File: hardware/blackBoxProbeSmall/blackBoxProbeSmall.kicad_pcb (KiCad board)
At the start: 4 copper layers, 44 x 29 mm, 79 parts, among them J1 USB-ID, J2 JTAG_2X05, J3 JTAG_2X05, J4 DevBoardUartInput, Q1 Q_NMOS_DUAL, Q2 Q_PMOS_DUAL, U1 MCP1702-MB, U2 USBLC6-2, U3 STM32F103CBT, U4 74X2T45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

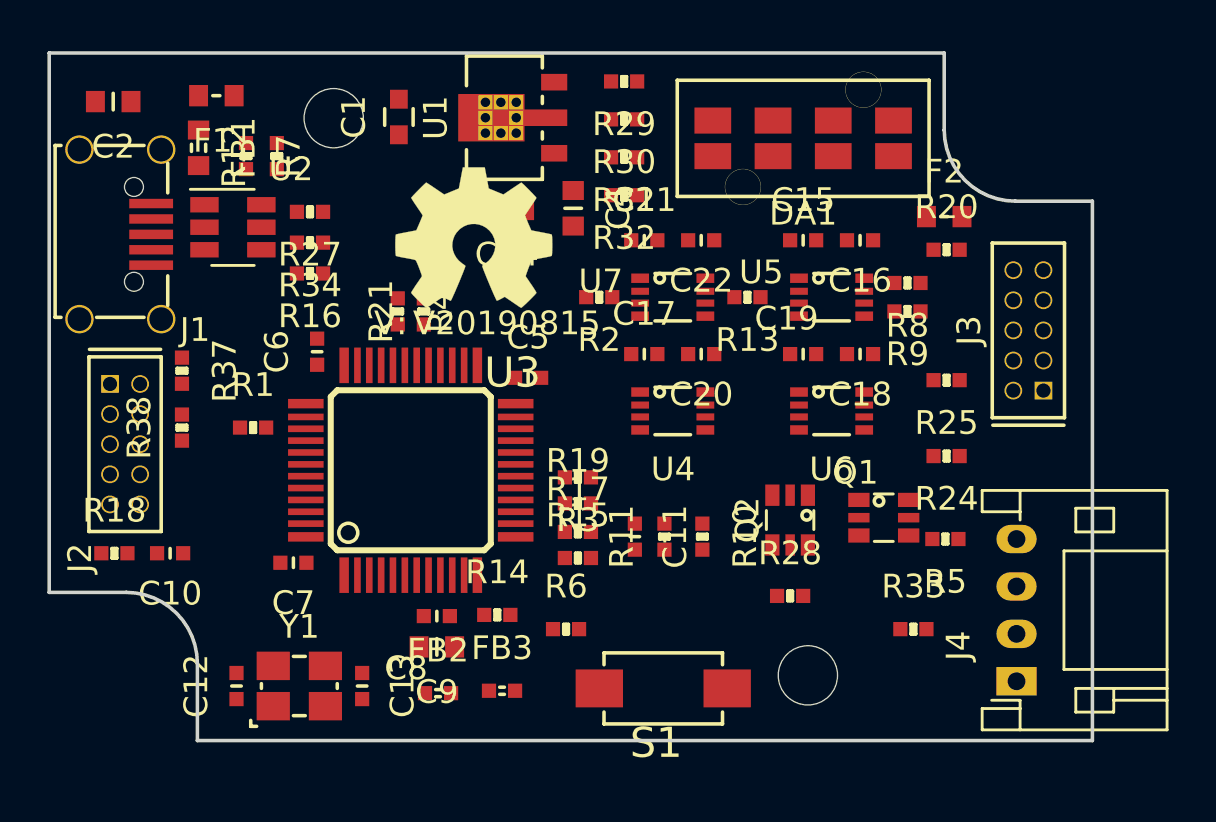
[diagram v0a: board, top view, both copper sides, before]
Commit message: initial component placement completed
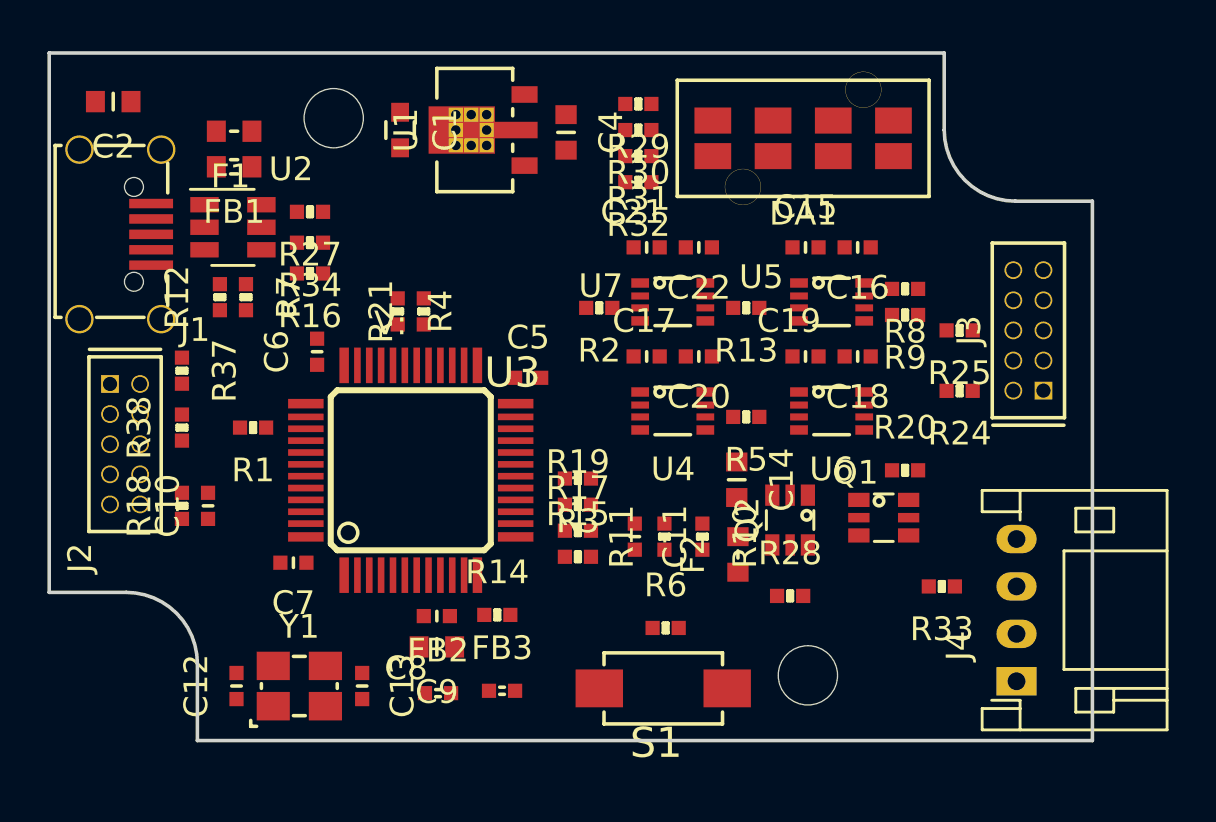
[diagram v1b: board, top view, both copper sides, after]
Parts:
- N1: moved to B.Cu
- moved F2 16.7 mm to (152.8, 106.0), turned to 90 degrees
- moved C14 15.0 mm to (152.7, 102.9), turned to 270 degrees
- moved R5 9.85 mm to (153.1, 100.2)
- moved R20 9.46 mm to (159.8, 102.5)
- moved R12 6.42 mm to (130.9, 95.2)
- moved R7 5.95 mm to (132.0, 95.2)
- moved R6 4.20 mm to (149.7, 109.2)
- moved R18 3.48 mm to (129.3, 104.0), turned to 90 degrees
- moved C4 3.21 mm to (145.5, 88.2)
- moved R24 2.80 mm to (162.1, 99.2)
- moved C10 2.56 mm to (130.4, 104.0), turned to 90 degrees
- moved R25 2.17 mm to (162.1, 96.6)
- moved R33 2.16 mm to (161.3, 107.4), turned to 180 degrees
- moved FB1 1.70 mm to (131.5, 89.7), turned to 180 degrees
- moved F1 1.68 mm to (131.5, 88.2)
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
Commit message: more layout
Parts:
- moved FB3 2.20 mm to (140.6, 111.8), turned to 270 degrees
- moved FB2 0.62 mm to (139.5, 111.8), turned to 270 degrees
- moved R16 0.30 mm to (134.7, 93.9)
- moved R27 0.11 mm to (134.7, 91.7)
- moved R34 0.11 mm to (134.7, 92.8)
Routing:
- net /VSS: track 0.00 -> 31.6 mm, vias 0 -> 10
- net /VUSB: track 0.00 -> 20.4 mm
- net Net-(C2-Pad2): track 0.00 -> 16.4 mm
- net /VDD: track 0.00 -> 8.06 mm, vias 0 -> 4
- net /VDDA: track 0.00 -> 4.61 mm
- net /VSSA: track 0.00 -> 4.52 mm
- net Net-(FB1-Pad2): track 0.00 -> 3.77 mm
- net Net-(R16-Pad2): track 0.00 -> 2.72 mm
- net /USB_D_C+: track 0.00 -> 2.52 mm
- net /USB_D_C-: track 0.00 -> 2.50 mm
- net Net-(F1-Pad2): track 0.00 -> 2.12 mm
- net Net-(R27-Pad2): track 0.00 -> 1.62 mm
- net /USB_V: track 0.00 -> 1.10 mm
- added copper zone on In2.Cu, net /VDD
- added copper zone on In1.Cu, net /VSS

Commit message: minor layout changes
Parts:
- moved R21 0.49 mm to (139.9, 95.6)
- moved R4 0.49 mm to (138.8, 95.6)
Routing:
- net /MCU_TMS: track 0.00 -> 11.1 mm
- net /MCU_TDI: track 0.00 -> 9.26 mm, vias 0 -> 2
- net /USB_D-: track 0.00 -> 8.18 mm
- net /USB_D+: track 0.00 -> 7.44 mm
- net /MCU_TCK: track 0.00 -> 7.19 mm
- net /MCU_TDO: track 0.00 -> 4.90 mm
- net /MCU_RST: track 0.00 -> 3.07 mm
- net Net-(R21-Pad1): track 0.00 -> 2.53 mm
- net /PROBE_I_RX: track 0.00 -> 1.99 mm
- net Net-(R1-Pad1): track 0.00 -> 1.68 mm
- net /VSS: track 31.6 -> 33.2 mm, vias 10 -> 12
- net /VDD: track 8.06 -> 9.46 mm, vias 4 -> 6
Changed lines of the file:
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@@
     (thickness 1.6)
     (drawings 10)
-    (tracks 143)
+    (tracks 207)
     (zones 0)
     (modules 79)
@@
   )
   (module SquantorRcl:R_0402_hand (layer F.Cu)
-    (at 139.5 95.8 90)
+    (at 139.95 95.6 90)
     (descr "Resistor SMD 0402, reflow soldering, Vishay (see dcrcw.pdf)")
     (tags "resistor 0402")
@@
   )
   (module SquantorRcl:R_0402_hand (layer F.Cu)
-    (at 138.4 95.8 270)
+    (at 138.85 95.6 270)
     (descr "Resistor SMD 0402, reflow soldering, Vishay (see dcrcw.pdf)")
     (tags "resistor 0402")
@@
   )
   (module SquantorRcl:R_0402_hand (layer F.Cu)
-    (at 132.3 100.7 180)
+    (at 132.3 100.75 180)
     (descr "Resistor SMD 0402, reflow soldering, Vishay (see dcrcw.pdf)")
     (tags "resistor 0402")
@@
   (segment (start 124.975 88.375) (end 125.65 87.7) (width 0.4) (layer F.Cu) (net 1))
   (segment (start 130.9 95.75) (end 132 95.75) (width 0.2) (layer F.Cu) (net 15))
+  (segment (start 134.525 99.69) (end 130.56 99.69) (width 0.2) (layer F.Cu) (net 16))
+  (segment (start 130.1 100.15) (end 129.3 100.15) (width 0.2) (layer F.Cu) (net 16))
+  (segment (start 130.56 99.69) (end 130.1 100.15) (width 0.2) (layer F.Cu) (net 16))
+  (segment (start 127.535 100.13) (end 128.73 100.13) (width 0.2) (layer F.Cu) (net 16))
+  (segment (start 128.75 100.15) (end 129.3 100.15) (width 0.2) (layer F.Cu) (net 16))
+  (segment (start 128.73 100.13) (end 128.75 100.15) (width 0.2) (layer F.Cu) (net 16))
+  (segment (start 134.525 100.25) (end 133.55 100.25) (width 0.2) (layer F.Cu) (net 17))
+  (segment (start 133.55 100.25) (end 133.4 100.1) (width 0.2) (layer F.Cu) (net 17))
+  (segment (start 133.4 100.1) (end 130.85 100.1) (width 0.2) (layer F.Cu) (net 17))
+  (via (at 130.55 100.4) (size 0.381) (drill 0.254) (layers F.Cu B.Cu) (net 17))
+  (segment (start 130.85 100.1) (end 130.55 100.4) (width 0.2) (layer F.Cu) (net 17))
+  (segment (start 130.55 100.4) (end 130.55 102.35) (width 0.2) (layer B.Cu) (net 17))
+  (via (at 130.55 102.35) (size 0.381) (drill 0.254) (layers F.Cu B.Cu) (net 17))
+  (segment (start 130.55 102.35) (end 128.8 102.35) (width 0.2) (layer F.Cu) (net 17))
+  (segment (start 128.48 102.67) (end 127.535 102.67) (width 0.2) (layer F.Cu) (net 17))
+  (segment (start 128.8 102.35) (end 128.48 102.67) (width 0.2) (layer F.Cu) (net 17))
+  (segment (start 135.85 99.4) (end 135.3 98.85) (width 0.2) (layer F.Cu) (net 18))
+  (segment (start 135.3 98.85) (end 129.3 98.85) (width 0.2) (layer F.Cu) (net 18))
+  (segment (start 136.95 99.4) (end 135.85 99.4) (width 0.2) (layer F.Cu) (net 18))
+  (segment (start 137.2 98.075) (end 137.2 99.15) (width 0.2) (layer F.Cu) (net 18))
+  (segment (start 137.2 99.15) (end 136.95 99.4) (width 0.2) (layer F.Cu) (net 18))
+  (segment (start 127.545 98.85) (end 127.535 98.86) (width 0.2) (layer F.Cu) (net 18))
+  (segment (start 129.3 98.85) (end 127.545 98.85) (width 0.2) (layer F.Cu) (net 18))
+  (segment (start 131.75 100.75) (end 131.3 100.75) (width 0.2) (layer F.Cu) (net 19))
+  (segment (start 131.3 100.75) (end 130.15 101.9) (width 0.2) (layer F.Cu) (net 19))
+  (segment (start 130.15 101.9) (end 128.7 101.9) (width 0.2) (layer F.Cu) (net 19))
+  (segment (start 128.2 101.4) (end 127.535 101.4) (width 0.2) (layer F.Cu) (net 19))
+  (segment (start 128.7 101.9) (end 128.2 101.4) (width 0.2) (layer F.Cu) (net 19))
+  (segment (start 127.535 103.94) (end 128.21 103.94) (width 0.2) (layer F.Cu) (net 20))
+  (segment (start 128.7 103.45) (end 129.3 103.45) (width 0.2) (layer F.Cu) (net 20))
+  (segment (start 128.21 103.94) (end 128.7 103.45) (width 0.2) (layer F.Cu) (net 20))
+  (segment (start 129.3 103.45) (end 130.4 103.45) (width 0.2) (layer F.Cu) (net 20))
+  (segment (start 137.7 96.949999) (end 137.7 98.075) (width 0.2) (layer F.Cu) (net 22))
+  (segment (start 137.725 96.924999) (end 137.7 96.949999) (width 0.2) (layer F.Cu) (net 22))
+  (segment (start 136.3068 92.475) (end 137.725 93.8932) (width 0.2) (layer F.Cu) (net 22))
+  (segment (start 135.975001 92.475) (end 136.3068 92.475) (width 0.2) (layer F.Cu) (net 22))
+  (segment (start 137.725 93.8932) (end 137.725 96.924999) (width 0.2) (layer F.Cu) (net 22))
+  (segment (start 135.650001 92.8) (end 135.975001 92.475) (width 0.2) (layer F.Cu) (net 22))
+  (segment (start 135.2 92.8) (end 135.650001 92.8) (width 0.2) (layer F.Cu) (net 22))
+  (segment (start 138.2 96.949999) (end 138.2 98.075) (width 0.2) (layer F.Cu) (net 32))
+  (segment (start 138.175 96.924999) (end 138.2 96.949999) (width 0.2) (layer F.Cu) (net 32))
+  (segment (start 136.4932 92.025) (end 138.175 93.7068) (width 0.2) (layer F.Cu) (net 32))
+  (segment (start 135.2 91.7) (end 135.650001 91.7) (width 0.2) (layer F.Cu) (net 32))
+  (segment (start 138.175 93.7068) (end 138.175 96.924999) (width 0.2) (layer F.Cu) (net 32))
+  (segment (start 135.975001 92.025) (end 136.4932 92.025) (width 0.2) (layer F.Cu) (net 32))
+  (segment (start 135.650001 91.7) (end 135.975001 92.025) (width 0.2) (layer F.Cu) (net 32))
+  (segment (start 138.7 98.075) (end 138.7 96.85) (width 0.2) (layer F.Cu) (net 37))
+  (segment (start 138.85 96.7) (end 138.85 96.15) (width 0.2) (layer F.Cu) (net 37))
+  (segment (start 138.7 96.85) (end 138.85 96.7) (width 0.2) (layer F.Cu) (net 37))
   (segment (start 129.75 93.2) (end 130.25 93.2) (width 0.2) (layer F.Cu) (net 40))
   (segment (start 128 92.55) (end 129.1 92.55) (width 0.2) (layer F.Cu) (net 40))
@@
   (via (at 138.8 112.3) (size 0.381) (drill 0.254) (layers F.Cu B.Cu) (net 49))
   (segment (start 139.5 112.3) (end 138.8 112.3) (width 0.4) (layer F.Cu) (net 49))
+  (via (at 130.05 100.9) (size 0.381) (drill 0.254) (layers F.Cu B.Cu) (net 49))
+  (segment (start 129.3 101.25) (end 129.7 101.25) (width 0.2) (layer F.Cu) (net 49))
+  (segment (start 129.7 101.25) (end 130.05 100.9) (width 0.2) (layer F.Cu) (net 49))
+  (via (at 130.4 105.25) (size 0.381) (drill 0.254) (layers F.Cu B.Cu) (net 49))
+  (segment (start 130.4 104.55) (end 130.4 105.25) (width 0.2) (layer F.Cu) (net 49))
   (segment (start 132.25 88.2) (end 132.9 88.2) (width 0.4) (layer F.Cu) (net 50))
   (segment (start 132.9 88.2) (end 134.3 89.6) (width 0.4) (layer F.Cu) (net 50))
@@
   (via (at 141.35 112.3) (size 0.381) (drill 0.254) (layers F.Cu B.Cu) (net 51))
   (segment (start 140.6 112.3) (end 141.35 112.3) (width 0.4) (layer F.Cu) (net 51))
+  (via (at 130 97.75) (size 0.381) (drill 0.254) (layers F.Cu B.Cu) (net 51))
+  (segment (start 129.3 97.75) (end 130 97.75) (width 0.2) (layer F.Cu) (net 51))
+  (via (at 129.3 105.25) (size 0.381) (drill 0.254) (layers F.Cu B.Cu) (net 51))
+  (segment (start 129.3 104.55) (end 129.3 105.25) (width 0.2) (layer F.Cu) (net 51))
   (segment (start 139.5 111.2) (end 139.5 110.75) (width 0.4) (layer F.Cu) (net 52))
   (segment (start 139.3 110.55) (end 139.3 109.95) (width 0.4) (layer F.Cu) (net 52))
@@
   (segment (start 130 89.7) (end 130.75 89.7) (width 0.4) (layer F.Cu) (net 55))
   (segment (start 129.25 90.45) (end 130 89.7) (width 0.4) (layer F.Cu) (net 55))
+  (segment (start 134.525 100.75) (end 132.85 100.75) (width 0.2) (layer F.Cu) (net 68))
+  (segment (start 139.2 98.075) (end 139.2 96.95) (width 0.2) (layer F.Cu) (net 80))
+  (segment (start 139.2 96.95) (end 139.35 96.8) (width 0.2) (layer F.Cu) (net 80))
+  (segment (start 139.35 96.8) (end 139.85 96.8) (width 0.2) (layer F.Cu) (net 80))
+  (segment (start 139.95 96.7) (end 139.95 96.15) (width 0.2) (layer F.Cu) (net 80))
+  (segment (start 139.85 96.8) (end 139.95 96.7) (width 0.2) (layer F.Cu) (net 80))
   (zone (net 49) (net_name /VSS) (layer In1.Cu) (hatch edge 0.508)
     (connect_pads (clearance 0.2))

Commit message: more layout
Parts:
- moved R6 6.91 mm to (143.6, 112.3)
- moved R1 0.30 mm to (132.0, 100.8)
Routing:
- net /VSS: track 33.2 -> 46.8 mm, vias 12 -> 14
- net Net-(C12-Pad1): track 0.00 -> 13.6 mm
- net /USB_V: track 1.10 -> 14.3 mm, vias 0 -> 2
- net /MCU_RST: track 3.07 -> 15.2 mm, vias 0 -> 2
- net /VDD: track 9.46 -> 21.0 mm, vias 6 -> 8
- net /USB_PU: track 0.00 -> 10.00 mm, vias 0 -> 2
- net Net-(C13-Pad1): track 0.00 -> 6.95 mm
- net /PROBE_I_RST: track 0.00 -> 3.40 mm
- net /BUTTON: track 0.00 -> 3.05 mm
- net /PROBE_I_TDO: track 0.00 -> 2.45 mm
- net Net-(R15-Pad1): track 0.00 -> 2.42 mm
- net Net-(R14-Pad1): track 0.00 -> 2.32 mm
- net Net-(R19-Pad1): track 0.00 -> 2.20 mm
- net Net-(R17-Pad1): track 0.00 -> 2.20 mm

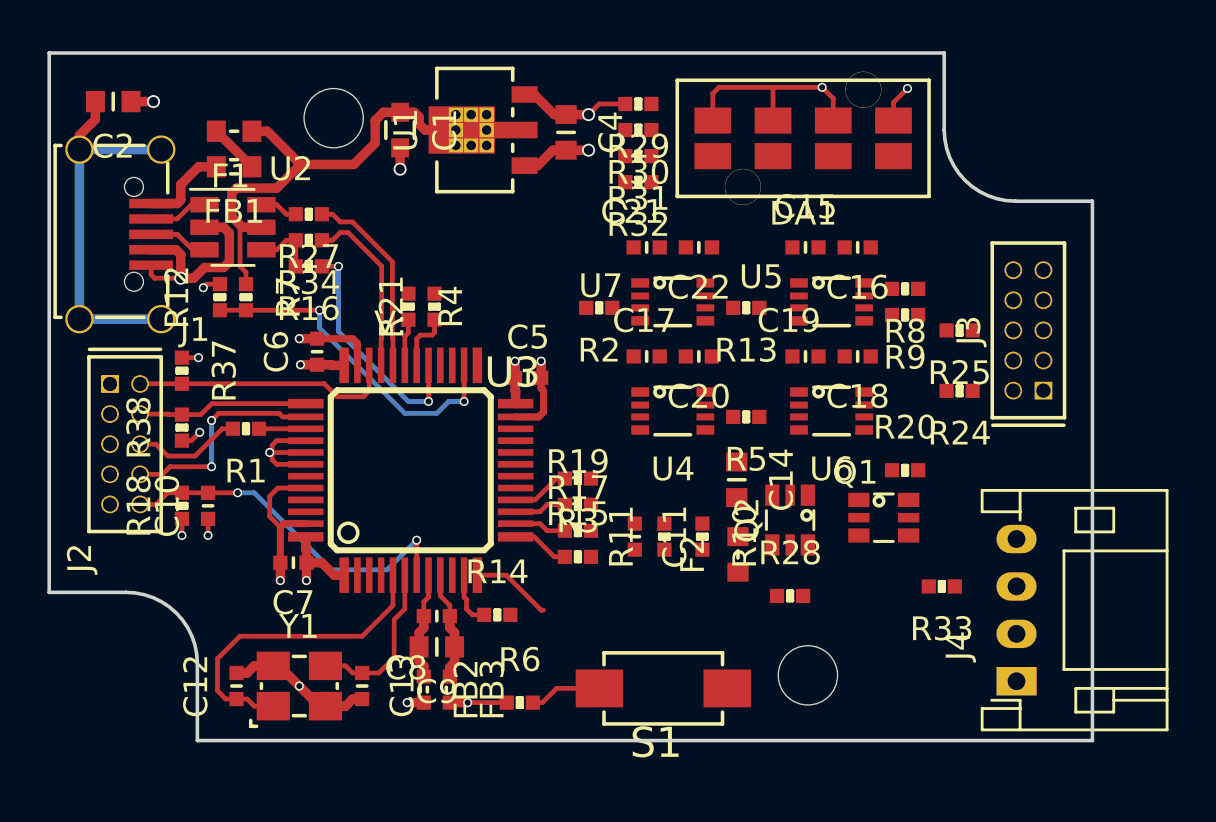
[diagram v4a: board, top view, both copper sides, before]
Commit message: more layout and some silk placement, need to move the microcontroller closer to the programming header to create more space
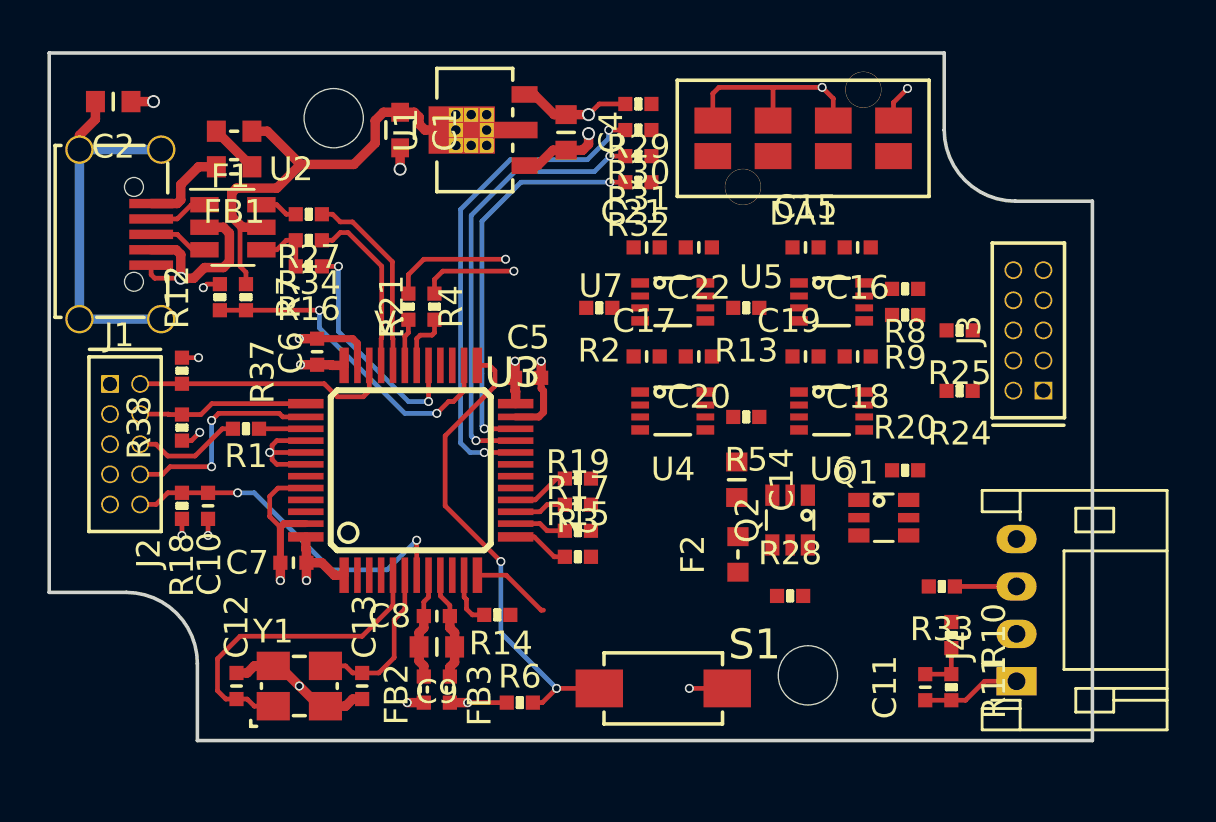
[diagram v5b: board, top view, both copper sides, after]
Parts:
- moved C11 13.8 mm to (160.7, 111.7), turned to 90 degrees
- moved R11 13.7 mm to (161.8, 111.7), turned to 270 degrees
- moved R10 11.3 mm to (161.8, 109.5)
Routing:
- net /LED0: track 0.00 -> 20.9 mm, vias 0 -> 2
- net /LED1: track 0.00 -> 18.8 mm, vias 0 -> 2
- net /BUTTON: track 3.05 -> 20.1 mm, vias 0 -> 2
- net /LED2: track 0.00 -> 16.8 mm, vias 0 -> 2
- net /VSS: track 46.8 -> 53.1 mm, vias 14 -> 15
- net Net-(R4-Pad1): track 0.00 -> 5.17 mm, vias 0 -> 1
- net /PROBE_I_TX: track 0.00 -> 4.09 mm, vias 0 -> 1
- net Net-(J4-Pad3): track 0.00 -> 2.60 mm
- net /TARGET_PWR_SENSE: track 0.00 -> 2.20 mm
